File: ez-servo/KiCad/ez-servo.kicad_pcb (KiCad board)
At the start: 4 copper layers, 20 x 20 mm, 14 parts, among them J2 SERVO, J3 VSEL, U1 TPS5430DDA

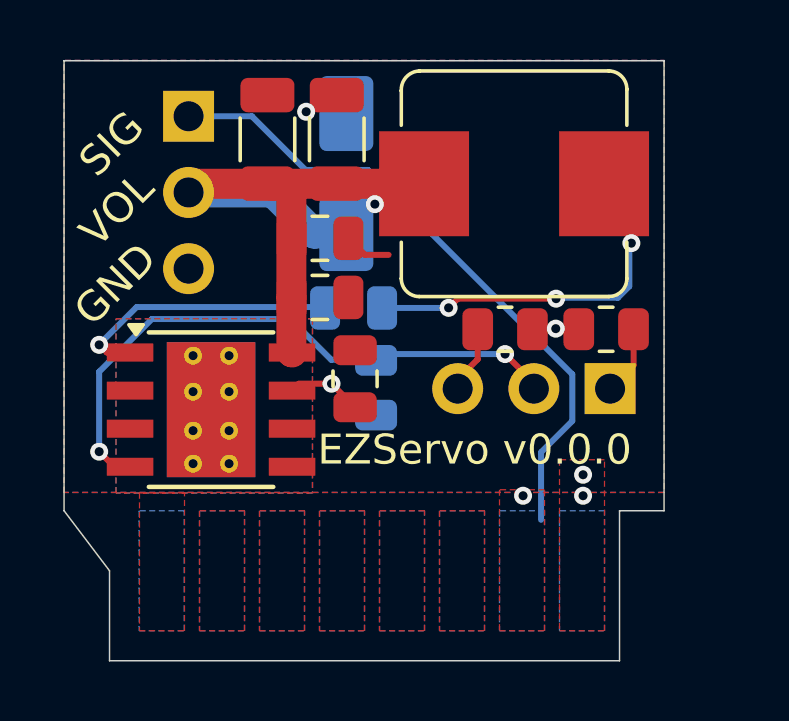
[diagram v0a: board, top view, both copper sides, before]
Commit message: fix: switch feedback resistor footprints for flexibility
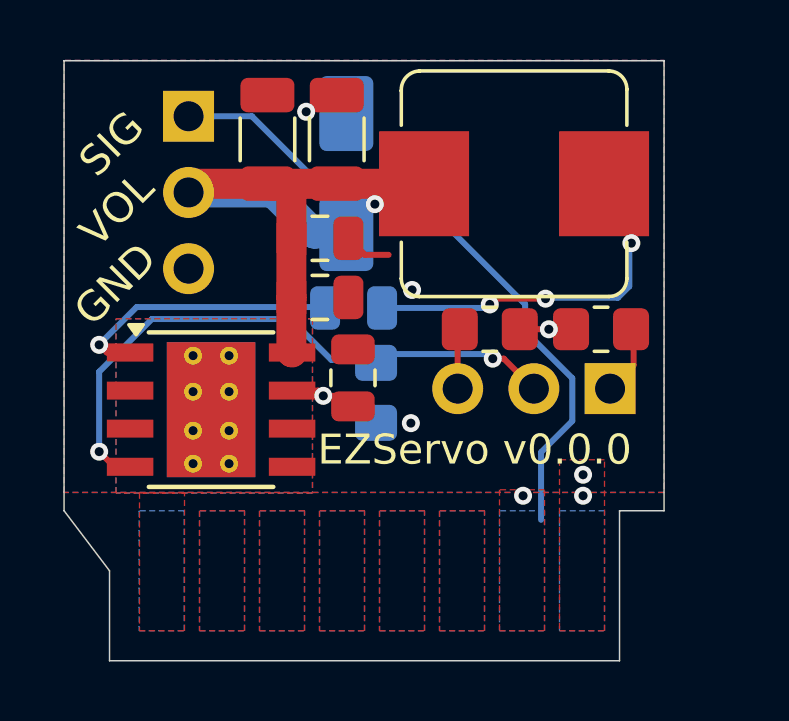
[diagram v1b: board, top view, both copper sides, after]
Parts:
- R1, R2, R3: footprint Resistor_SMD:R_0805_2012Metric -> Resistor_SMD:R_0805_2012Metric_Pad1.20x1.40mm_HandSolder
- moved R3 0.51 mm to (39.2, 34.0)
- moved R1 0.17 mm to (42.9, 34.0)
- moved R2 0.17 mm to (35.4, 36.1)
- moved C1 0.08 mm to (34.6, 35.6)
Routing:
- net GND: vias 2 -> 4
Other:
- board text added: "1.5mm pins 0.5mm spacing 8x each side 4mm tall 1mm from bottom 1mm from keyed edge 7.5mm thick at heatsink"
- board text removed: "1.5mm pins 0.5mm spacing 8x each side 4mm tall 1mm from bottom 1mm from keyed edge 7.5mm thick"
